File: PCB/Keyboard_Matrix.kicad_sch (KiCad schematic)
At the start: 249 parts

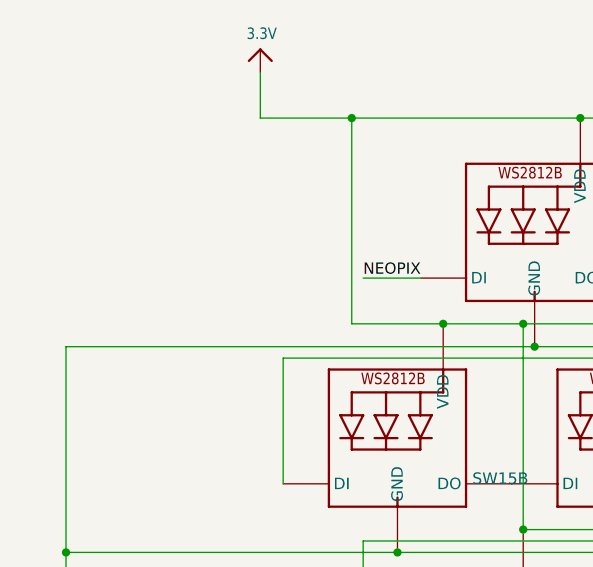
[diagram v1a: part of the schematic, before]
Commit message: Redo microcontroller layout
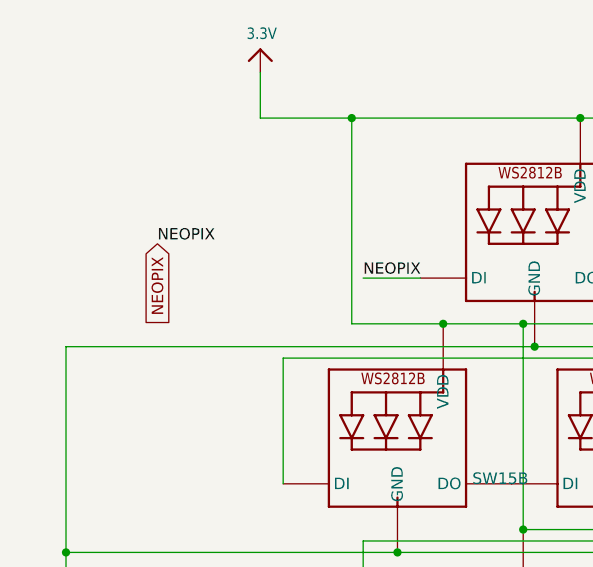
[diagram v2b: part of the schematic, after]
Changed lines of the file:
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@@
     (effects (font (size 1.2446 1.2446)) (justify left bottom))
+  )
+  (label "NEOPIX" (at -20.32 233.68 0) (fields_autoplaced)
+    (effects (font (size 1.2446 1.2446)) (justify left bottom))
+  )
+  (global_label "NEOPIX" (shape input) (at -20.32 233.68 270) (fields_autoplaced)
+    (effects (font (size 1.27 1.27)) (justify right))
+    (property "Intersheetrefs" "${INTERSHEET_REFS}" (at -20.32 243.4801 90)
+      (effects (font (size 1.27 1.27)) (justify right) hide)
+    )
   )
   (symbol (lib_id "JohnDeere:MX_NEO") (at 102.87 38.1 0) (unit 1)

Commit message: Columns
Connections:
- net Row: now reaches SW16.1, SW17.1, SW18.1, SW19.1, SW20.1, SW21.1, SW22.1, SW23.1, SW24.1, SW25.1, SW26.1, SW27.1, SW28.1, SW29.1, SW30.1, SW31.1
- net Row: now also SW1.1, SW10.1, SW11.1, SW12.1, SW13.1, SW14.1, SW15.1, SW2.1, SW3.1, SW32.1, SW33.1, SW34.1, SW35.1, SW36.1, SW37.1, SW38.1, SW39.1, SW4.1, SW40.1, SW41.1, SW42.1, SW43.1, SW44.1, SW45.1, SW46.1, SW47.1, SW48.1, SW49.1, SW5.1, SW50.1, SW51.1, SW52.1, SW53.1, SW54.1, SW55.1, SW56.1, SW57.1, SW58.1, SW59.1, SW6.1, SW60.1, SW61.1, SW62.1, SW63.1, SW64.1, SW65.1, SW66.1, SW67.1, SW68.1, SW69.1, SW7.1, SW70.1, SW71.1, SW72.1, SW73.1, SW74.1, SW75.1, SW76.1, SW77.1, SW78.1, SW79.1, SW8.1, SW80.1, SW81.1, SW82.1, SW83.1, SW9.1
- net Col: now reaches D17.1 (K), D2.1 (K), D33.1 (K), D49.1 (K), D62.1 (K), D75.1 (K)
- net Col: now also D1.1 (K), D10.1 (K), D11.1 (K), D12.1 (K), D13.1 (K), D14.1 (K), D15.1 (K), D16.1 (K), D18.1 (K), D19.1 (K), D20.1 (K), D21.1 (K), D22.1 (K), D23.1 (K), D24.1 (K), D25.1 (K), D26.1 (K), D27.1 (K), D28.1 (K), D29.1 (K), D3.1 (K), D30.1 (K), D31.1 (K), D32.1 (K), D34.1 (K), D35.1 (K), D36.1 (K), D37.1 (K), D38.1 (K), D39.1 (K), D4.1 (K), D40.1 (K), D41.1 (K), D42.1 (K), D43.1 (K), D44.1 (K), D45.1 (K), D46.1 (K), D47.1 (K), D48.1 (K), D5.1 (K), D50.1 (K), D51.1 (K), D52.1 (K), D53.1 (K), D54.1 (K), D55.1 (K), D56.1 (K), D57.1 (K), D58.1 (K), D59.1 (K), D6.1 (K), D60.1 (K), D61.1 (K), D63.1 (K), D64.1 (K), D65.1 (K), D66.1 (K), D67.1 (K), D68.1 (K), D69.1 (K), D7.1 (K), D70.1 (K), D71.1 (K), D72.1 (K), D73.1 (K), D74.1 (K), D76.1 (K), D77.1 (K), D78.1 (K), D79.1 (K), D8.1 (K), D80.1 (K), D81.1 (K), D82.1 (K), D83.1 (K), D9.1 (K)

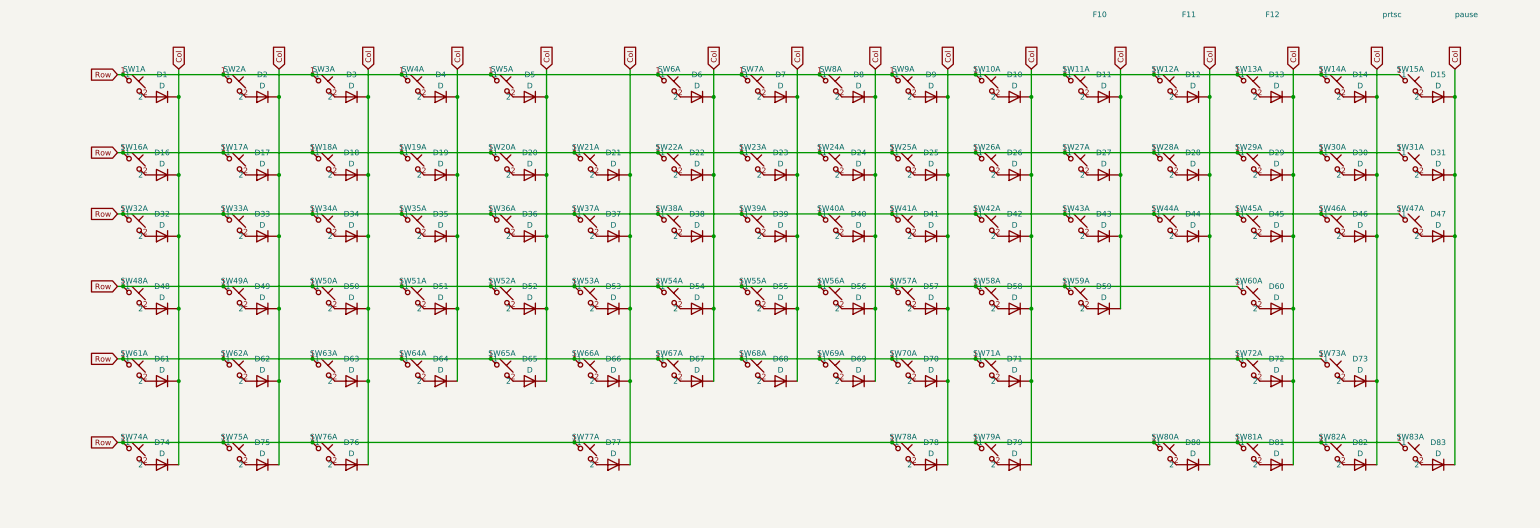
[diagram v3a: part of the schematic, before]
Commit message: update matrix nets and add swd footprint
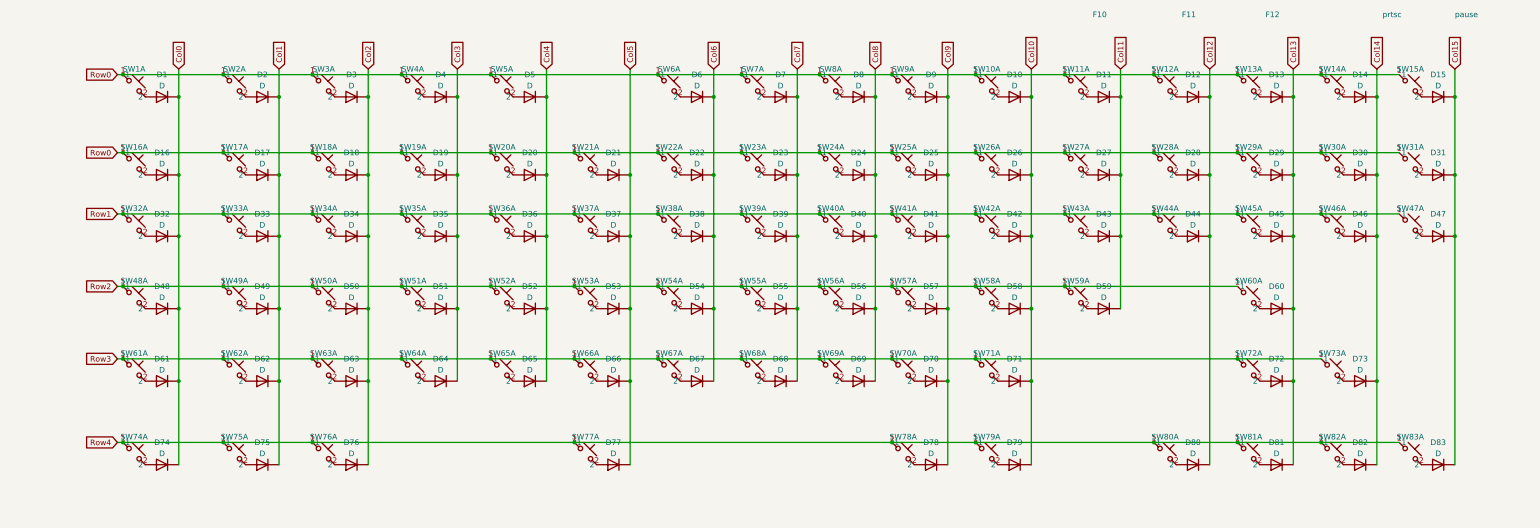
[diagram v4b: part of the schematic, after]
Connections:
- removed net Col: D1.1 (K), D10.1 (K), D11.1 (K), D12.1 (K), D13.1 (K), D14.1 (K), D15.1 (K), D16.1 (K), D17.1 (K), D18.1 (K), D19.1 (K), D2.1 (K), D20.1 (K), D21.1 (K), D22.1 (K), D23.1 (K), D24.1 (K), D25.1 (K), D26.1 (K), D27.1 (K), D28.1 (K), D29.1 (K), D3.1 (K), D30.1 (K), D31.1 (K), D32.1 (K), D33.1 (K), D34.1 (K), D35.1 (K), D36.1 (K), D37.1 (K), D38.1 (K), D39.1 (K), D4.1 (K), D40.1 (K), D41.1 (K), D42.1 (K), D43.1 (K), D44.1 (K), D45.1 (K), D46.1 (K), D47.1 (K), D48.1 (K), D49.1 (K), D5.1 (K), D50.1 (K), D51.1 (K), D52.1 (K), D53.1 (K), D54.1 (K), D55.1 (K), D56.1 (K), D57.1 (K), D58.1 (K), D59.1 (K), D6.1 (K), D60.1 (K), D61.1 (K), D62.1 (K), D63.1 (K), D64.1 (K), D65.1 (K), D66.1 (K), D67.1 (K), D68.1 (K), D69.1 (K), D7.1 (K), D70.1 (K), D71.1 (K), D72.1 (K), D73.1 (K), D74.1 (K), D75.1 (K), D76.1 (K), D77.1 (K), D78.1 (K), D79.1 (K), D8.1 (K), D80.1 (K), D81.1 (K), D82.1 (K), D83.1 (K), D9.1 (K)
- removed net Row: SW1.1, SW10.1, SW11.1, SW12.1, SW13.1, SW14.1, SW15.1, SW16.1, SW17.1, SW18.1, SW19.1, SW2.1, SW20.1, SW21.1, SW22.1, SW23.1, SW24.1, SW25.1, SW26.1, SW27.1, SW28.1, SW29.1, SW3.1, SW30.1, SW31.1, SW32.1, SW33.1, SW34.1, SW35.1, SW36.1, SW37.1, SW38.1, SW39.1, SW4.1, SW40.1, SW41.1, SW42.1, SW43.1, SW44.1, SW45.1, SW46.1, SW47.1, SW48.1, SW49.1, SW5.1, SW50.1, SW51.1, SW52.1, SW53.1, SW54.1, SW55.1, SW56.1, SW57.1, SW58.1, SW59.1, SW6.1, SW60.1, SW61.1, SW62.1, SW63.1, SW64.1, SW65.1, SW66.1, SW67.1, SW68.1, SW69.1, SW7.1, SW70.1, SW71.1, SW72.1, SW73.1, SW74.1, SW75.1, SW76.1, SW77.1, SW78.1, SW79.1, SW8.1, SW80.1, SW81.1, SW82.1, SW83.1, SW9.1
- new net Col0: D1.1 (K), D16.1 (K), D32.1 (K), D48.1 (K), D61.1 (K), D74.1 (K)
- new net Col1: D17.1 (K), D2.1 (K), D33.1 (K), D49.1 (K), D62.1 (K), D75.1 (K)
- new net Col10: D10.1 (K), D26.1 (K), D42.1 (K), D58.1 (K), D71.1 (K), D79.1 (K)
- new net Col11: D11.1 (K), D27.1 (K), D43.1 (K), D59.1 (K)
- new net Col12: D12.1 (K), D28.1 (K), D44.1 (K), D80.1 (K)
- new net Col13: D13.1 (K), D29.1 (K), D45.1 (K), D60.1 (K), D72.1 (K), D81.1 (K)
- new net Col14: D14.1 (K), D30.1 (K), D46.1 (K), D73.1 (K), D82.1 (K)
- new net Col15: D15.1 (K), D31.1 (K), D47.1 (K), D83.1 (K)
- new net Col2: D18.1 (K), D3.1 (K), D34.1 (K), D50.1 (K), D63.1 (K), D76.1 (K)
- new net Col3: D19.1 (K), D35.1 (K), D4.1 (K), D51.1 (K), D64.1 (K)
- new net Col4: D20.1 (K), D36.1 (K), D5.1 (K), D52.1 (K), D65.1 (K)
- new net Col5: D21.1 (K), D37.1 (K), D53.1 (K), D66.1 (K), D77.1 (K)
- new net Col6: D22.1 (K), D38.1 (K), D54.1 (K), D6.1 (K), D67.1 (K)
- new net Col7: D23.1 (K), D39.1 (K), D55.1 (K), D68.1 (K), D7.1 (K)
- new net Col8: D24.1 (K), D40.1 (K), D56.1 (K), D69.1 (K), D8.1 (K)
- new net Col9: D25.1 (K), D41.1 (K), D57.1 (K), D70.1 (K), D78.1 (K), D9.1 (K)
- new net Row0: SW1.1, SW10.1, SW11.1, SW12.1, SW13.1, SW14.1, SW15.1, SW16.1, SW17.1, SW18.1, SW19.1, SW2.1, SW20.1, SW21.1, SW22.1, SW23.1, SW24.1, SW25.1, SW26.1, SW27.1, SW28.1, SW29.1, SW3.1, SW30.1, SW31.1, SW4.1, SW5.1, SW6.1, SW7.1, SW8.1, SW9.1
- new net Row1: SW32.1, SW33.1, SW34.1, SW35.1, SW36.1, SW37.1, SW38.1, SW39.1, SW40.1, SW41.1, SW42.1, SW43.1, SW44.1, SW45.1, SW46.1, SW47.1
- new net Row2: SW48.1, SW49.1, SW50.1, SW51.1, SW52.1, SW53.1, SW54.1, SW55.1, SW56.1, SW57.1, SW58.1, SW59.1, SW60.1
- new net Row3: SW61.1, SW62.1, SW63.1, SW64.1, SW65.1, SW66.1, SW67.1, SW68.1, SW69.1, SW70.1, SW71.1, SW72.1, SW73.1
- new net Row4: SW74.1, SW75.1, SW76.1, SW77.1, SW78.1, SW79.1, SW80.1, SW81.1, SW82.1, SW83.1
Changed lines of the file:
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@@
     (effects (font (size 1.2446 1.2446)) (justify left bottom))
   )
-  (global_label "Row" (shape input) (at 15.24 49.53 180) (fields_autoplaced)
+  (global_label "Row1" (shape input) (at 15.24 49.53 180) (fields_autoplaced)
     (effects (font (size 1.27 1.27)) (justify right))
-    (property "Intersheetrefs" "${INTERSHEET_REFS}" (at 8.5847 49.53 0)
+    (property "Intersheetrefs" "${INTERSHEET_REFS}" (at 7.3752 49.53 0)
       (effects (font (size 1.27 1.27)) (justify right) hide)
     )
   )
-  (global_label "Col" (shape input) (at 302.26 16.51 90) (fields_autoplaced)
+  (global_label "Col14" (shape input) (at 302.26 16.51 90) (fields_autoplaced)
     (effects (font (size 1.27 1.27)) (justify left))
-    (property "Intersheetrefs" "${INTERSHEET_REFS}" (at 302.26 10.52 90)
+    (property "Intersheetrefs" "${INTERSHEET_REFS}" (at 302.26 8.101 90)
       (effects (font (size 1.27 1.27)) (justify left) hide)
     )
   )
-  (global_label "Col" (shape input) (at 243.84 16.51 90) (fields_autoplaced)
+  (global_label "Col11" (shape input) (at 243.84 16.51 90) (fields_autoplaced)
     (effects (font (size 1.27 1.27)) (justify left))
-    (property "Intersheetrefs" "${INTERSHEET_REFS}" (at 243.84 10.52 90)
+    (property "Intersheetrefs" "${INTERSHEET_REFS}" (at 243.84 8.101 90)
       (effects (font (size 1.27 1.27)) (justify left) hide)
     )
   )
-  (global_label "Col" (shape input) (at 132.08 16.51 90) (fields_autoplaced)
+  (global_label "Col5" (shape input) (at 132.08 16.51 90) (fields_autoplaced)
     (effects (font (size 1.27 1.27)) (justify left))
-    (property "Intersheetrefs" "${INTERSHEET_REFS}" (at 132.08 10.52 90)
+    (property "Intersheetrefs" "${INTERSHEET_REFS}" (at 132.08 9.3105 90)
       (effects (font (size 1.27 1.27)) (justify left) hide)
     )
   )
-  (global_label "Col" (shape input) (at 264.16 16.51 90) (fields_autoplaced)
+  (global_label "Col12" (shape input) (at 264.16 16.51 90) (fields_autoplaced)
     (effects (font (size 1.27 1.27)) (justify left))
-    (property "Intersheetrefs" "${INTERSHEET_REFS}" (at 264.16 10.52 90)
+    (property "Intersheetrefs" "${INTERSHEET_REFS}" (at 264.16 8.101 90)
       (effects (font (size 1.27 1.27)) (justify left) hide)
     )
@@
     )
   )
-  (global_label "Col" (shape input) (at 223.52 16.51 90) (fields_autoplaced)
+  (global_label "Col10" (shape input) (at 223.52 16.51 90) (fields_autoplaced)
     (effects (font (size 1.27 1.27)) (justify left))
-    (property "Intersheetrefs" "${INTERSHEET_REFS}" (at 223.52 10.52 90)
+    (property "Intersheetrefs" "${INTERSHEET_REFS}" (at 223.52 8.101 90)
       (effects (font (size 1.27 1.27)) (justify left) hide)
     )
   )
-  (global_label "Row" (shape input) (at 15.24 66.04 180) (fields_autoplaced)
+  (global_label "Row2" (shape input) (at 15.24 66.04 180) (fields_autoplaced)
     (effects (font (size 1.27 1.27)) (justify right))
-    (property "Intersheetrefs" "${INTERSHEET_REFS}" (at 8.5847 66.04 0)
+    (property "Intersheetrefs" "${INTERSHEET_REFS}" (at 7.3752 66.04 0)
       (effects (font (size 1.27 1.27)) (justify right) hide)
     )
   )
-  (global_label "Col" (shape input) (at 72.39 16.51 90) (fields_autoplaced)
+  (global_label "Col2" (shape input) (at 72.39 16.51 90) (fields_autoplaced)
     (effects (font (size 1.27 1.27)) (justify left))
-    (property "Intersheetrefs" "${INTERSHEET_REFS}" (at 72.39 10.52 90)
+    (property "Intersheetrefs" "${INTERSHEET_REFS}" (at 72.39 9.3105 90)
       (effects (font (size 1.27 1.27)) (justify left) hide)
     )
   )
-  (global_label "Row" (shape input) (at 15.24 82.55 180) (fields_autoplaced)
+  (global_label "Row3" (shape input) (at 15.24 82.55 180) (fields_autoplaced)
     (effects (font (size 1.27 1.27)) (justify right))
-    (property "Intersheetrefs" "${INTERSHEET_REFS}" (at 8.5847 82.55 0)
+    (property "Intersheetrefs" "${INTERSHEET_REFS}" (at 7.3752 82.55 0)
       (effects (font (size 1.27 1.27)) (justify right) hide)
     )
   )
-  (global_label "Row" (shape input) (at 15.24 35.56 180) (fields_autoplaced)
+  (global_label "Row0" (shape input) (at 15.24 35.56 180) (fields_autoplaced)
     (effects (font (size 1.27 1.27)) (justify right))
-    (property "Intersheetrefs" "${INTERSHEET_REFS}" (at 8.5847 35.56 0)
+    (property "Intersheetrefs" "${INTERSHEET_REFS}" (at 7.3752 35.56 0)
       (effects (font (size 1.27 1.27)) (justify right) hide)
     )
   )
-  (global_label "Col" (shape input) (at 92.71 16.51 90) (fields_autoplaced)
+  (global_label "Col3" (shape input) (at 92.71 16.51 90) (fields_autoplaced)
     (effects (font (size 1.27 1.27)) (justify left))
-    (property "Intersheetrefs" "${INTERSHEET_REFS}" (at 92.71 10.52 90)
+    (property "Intersheetrefs" "${INTERSHEET_REFS}" (at 92.71 9.3105 90)
       (effects (font (size 1.27 1.27)) (justify left) hide)
     )
   )
-  (global_label "Row" (shape input) (at 15.24 101.6 180) (fields_autoplaced)
+  (global_label "Row4" (shape input) (at 15.24 101.6 180) (fields_autoplaced)
     (effects (font (size 1.27 1.27)) (justify right))
-    (property "Intersheetrefs" "${INTERSHEET_REFS}" (at 8.5847 101.6 0)
+    (property "Intersheetrefs" "${INTERSHEET_REFS}" (at 7.3752 101.6 0)
       (effects (font (size 1.27 1.27)) (justify right) hide)
     )
   )
-  (global_label "Col" (shape input) (at 113.03 16.51 90) (fields_autoplaced)
+  (global_label "Col4" (shape input) (at 113.03 16.51 90) (fields_autoplaced)
     (effects (font (size 1.27 1.27)) (justify left))
-    (property "Intersheetrefs" "${INTERSHEET_REFS}" (at 113.03 10.52 90)
+    (property "Intersheetrefs" "${INTERSHEET_REFS}" (at 113.03 9.3105 90)
       (effects (font (size 1.27 1.27)) (justify left) hide)
     )
   )
-  (global_label "Col" (shape input) (at 29.21 16.51 90) (fields_autoplaced)
+  (global_label "Col0" (shape input) (at 29.21 16.51 90) (fields_autoplaced)
     (effects (font (size 1.27 1.27)) (justify left))
-    (property "Intersheetrefs" "${INTERSHEET_REFS}" (at 29.21 10.52 90)
+    (property "Intersheetrefs" "${INTERSHEET_REFS}" (at 29.21 9.3105 90)
       (effects (font (size 1.27 1.27)) (justify left) hide)
     )
   )
-  (global_label "Col" (shape input) (at 204.47 16.51 90) (fields_autoplaced)
+  (global_label "Col9" (shape input) (at 204.47 16.51 90) (fields_autoplaced)
     (effects (font (size 1.27 1.27)) (justify left))
-    (property "Intersheetrefs" "${INTERSHEET_REFS}" (at 204.47 10.52 90)
+    (property "Intersheetrefs" "${INTERSHEET_REFS}" (at 204.47 9.3105 90)
       (effects (font (size 1.27 1.27)) (justify left) hide)
     )
   )
-  (global_label "Col" (shape input) (at 170.18 16.51 90) (fields_autoplaced)
+  (global_label "Col7" (shape input) (at 170.18 16.51 90) (fields_autoplaced)
     (effects (font (size 1.27 1.27)) (justify left))
-    (property "Intersheetrefs" "${INTERSHEET_REFS}" (at 170.18 10.52 90)
+    (property "Intersheetrefs" "${INTERSHEET_REFS}" (at 170.18 9.3105 90)
       (effects (font (size 1.27 1.27)) (justify left) hide)
     )
   )
-  (global_label "Col" (shape input) (at 283.21 16.51 90) (fields_autoplaced)
+  (global_label "Col13" (shape input) (at 283.21 16.51 90) (fields_autoplaced)
     (effects (font (size 1.27 1.27)) (justify left))
-    (property "Intersheetrefs" "${INTERSHEET_REFS}" (at 283.21 10.52 90)
+    (property "Intersheetrefs" "${INTERSHEET_REFS}" (at 283.21 8.101 90)
       (effects (font (size 1.27 1.27)) (justify left) hide)
     )
   )
-  (global_label "Col" (shape input) (at 320.04 16.51 90) (fields_autoplaced)
+  (global_label "Col15" (shape input) (at 320.04 16.51 90) (fields_autoplaced)
     (effects (font (size 1.27 1.27)) (justify left))
-    (property "Intersheetrefs" "${INTERSHEET_REFS}" (at 320.04 10.52 90)
+    (property "Intersheetrefs" "${INTERSHEET_REFS}" (at 320.04 8.101 90)
       (effects (font (size 1.27 1.27)) (justify left) hide)
     )
   )
-  (global_label "Col" (shape input) (at 187.96 16.51 90) (fields_autoplaced)
+  (global_label "Col8" (shape input) (at 187.96 16.51 90) (fields_autoplaced)
     (effects (font (size 1.27 1.27)) (justify left))
-    (property "Intersheetrefs" "${INTERSHEET_REFS}" (at 187.96 10.52 90)
+    (property "Intersheetrefs" "${INTERSHEET_REFS}" (at 187.96 9.3105 90)
       (effects (font (size 1.27 1.27)) (justify left) hide)
     )
   )
-  (global_label "Col" (shape input) (at 52.07 16.51 90) (fields_autoplaced)
+  (global_label "Col1" (shape input) (at 52.07 16.51 90) (fields_autoplaced)
     (effects (font (size 1.27 1.27)) (justify left))
-    (property "Intersheetrefs" "${INTERSHEET_REFS}" (at 52.07 10.52 90)
+    (property "Intersheetrefs" "${INTERSHEET_REFS}" (at 52.07 9.3105 90)
       (effects (font (size 1.27 1.27)) (justify left) hide)
     )
   )
-  (global_label "Col" (shape input) (at 151.13 16.51 90) (fields_autoplaced)
+  (global_label "Col6" (shape input) (at 151.13 16.51 90) (fields_autoplaced)
     (effects (font (size 1.27 1.27)) (justify left))
-    (property "Intersheetrefs" "${INTERSHEET_REFS}" (at 151.13 10.52 90)
+    (property "Intersheetrefs" "${INTERSHEET_REFS}" (at 151.13 9.3105 90)
       (effects (font (size 1.27 1.27)) (justify left) hide)
     )
   )
-  (global_label "Row" (shape input) (at 15.24 17.78 180) (fields_autoplaced)
+  (global_label "Row0" (shape input) (at 15.24 17.78 180) (fields_autoplaced)
     (effects (font (size 1.27 1.27)) (justify right))
-    (property "Intersheetrefs" "${INTERSHEET_REFS}" (at 8.5847 17.78 0)
+    (property "Intersheetrefs" "${INTERSHEET_REFS}" (at 7.3752 17.78 0)
       (effects (font (size 1.27 1.27)) (justify right) hide)
     )

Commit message: Matrix work
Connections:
- net Row0: no longer SW16.1, SW17.1, SW18.1, SW19.1, SW20.1, SW21.1, SW22.1, SW23.1, SW24.1, SW25.1, SW26.1, SW27.1, SW28.1, SW29.1, SW30.1, SW31.1
- net Row1: now also SW16.1, SW17.1, SW18.1, SW19.1, SW20.1, SW21.1, SW22.1, SW23.1, SW24.1, SW25.1, SW26.1, SW27.1, SW28.1, SW29.1, SW30.1, SW31.1; no longer SW32.1, SW33.1, SW34.1, SW35.1, SW36.1, SW37.1, SW38.1, SW39.1, SW40.1, SW41.1, SW42.1, SW43.1, SW44.1, SW45.1, SW46.1, SW47.1
- net Row2: now also SW32.1, SW33.1, SW34.1, SW35.1, SW36.1, SW37.1, SW38.1, SW39.1, SW40.1, SW41.1, SW42.1, SW43.1, SW44.1, SW45.1, SW46.1, SW47.1; no longer SW48.1, SW49.1, SW50.1, SW51.1, SW52.1, SW53.1, SW54.1, SW55.1, SW56.1, SW57.1, SW58.1, SW59.1, SW60.1
- net Row3: now also SW48.1, SW49.1, SW50.1, SW51.1, SW52.1, SW53.1, SW54.1, SW55.1, SW56.1, SW57.1, SW58.1, SW59.1, SW60.1; no longer SW61.1, SW62.1, SW63.1, SW64.1, SW65.1, SW66.1, SW67.1, SW68.1, SW69.1, SW70.1, SW71.1, SW72.1, SW73.1
- net Row4: now also SW61.1, SW62.1, SW63.1, SW64.1, SW65.1, SW66.1, SW67.1, SW68.1, SW69.1, SW70.1, SW71.1, SW72.1, SW73.1; no longer SW74.1, SW75.1, SW76.1, SW77.1, SW78.1, SW79.1, SW80.1, SW81.1, SW82.1, SW83.1
- new net Row5: SW74.1, SW75.1, SW76.1, SW77.1, SW78.1, SW79.1, SW80.1, SW81.1, SW82.1, SW83.1
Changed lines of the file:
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@@
     (effects (font (size 1.2446 1.2446)) (justify left bottom))
   )
-  (global_label "Row1" (shape input) (at 15.24 49.53 180) (fields_autoplaced)
+  (global_label "Row2" (shape input) (at 15.24 49.53 180) (fields_autoplaced)
     (effects (font (size 1.27 1.27)) (justify right))
     (property "Intersheetrefs" "${INTERSHEET_REFS}" (at 7.3752 49.53 0)
@@
     )
   )
-  (global_label "Row2" (shape input) (at 15.24 66.04 180) (fields_autoplaced)
+  (global_label "Row3" (shape input) (at 15.24 66.04 180) (fields_autoplaced)
     (effects (font (size 1.27 1.27)) (justify right))
     (property "Intersheetrefs" "${INTERSHEET_REFS}" (at 7.3752 66.04 0)
@@
     )
   )
-  (global_label "Row3" (shape input) (at 15.24 82.55 180) (fields_autoplaced)
+  (global_label "Row4" (shape input) (at 15.24 82.55 180) (fields_autoplaced)
     (effects (font (size 1.27 1.27)) (justify right))
     (property "Intersheetrefs" "${INTERSHEET_REFS}" (at 7.3752 82.55 0)
@@
     )
   )
-  (global_label "Row0" (shape input) (at 15.24 35.56 180) (fields_autoplaced)
+  (global_label "Row1" (shape input) (at 15.24 35.56 180) (fields_autoplaced)
     (effects (font (size 1.27 1.27)) (justify right))
     (property "Intersheetrefs" "${INTERSHEET_REFS}" (at 7.3752 35.56 0)
@@
     )
   )
-  (global_label "Row4" (shape input) (at 15.24 101.6 180) (fields_autoplaced)
+  (global_label "Row5" (shape input) (at 15.24 101.6 180) (fields_autoplaced)
     (effects (font (size 1.27 1.27)) (justify right))
     (property "Intersheetrefs" "${INTERSHEET_REFS}" (at 7.3752 101.6 0)
